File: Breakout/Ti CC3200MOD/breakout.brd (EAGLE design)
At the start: 52.5 x 42.5 mm, 68 parts, among them Q1 16Mhz, U1 TPS63001DRCT, U11 XL, U12 TMP006, U2 MCP73871-2CCI/ML, U5 93LC46BT-I/OT

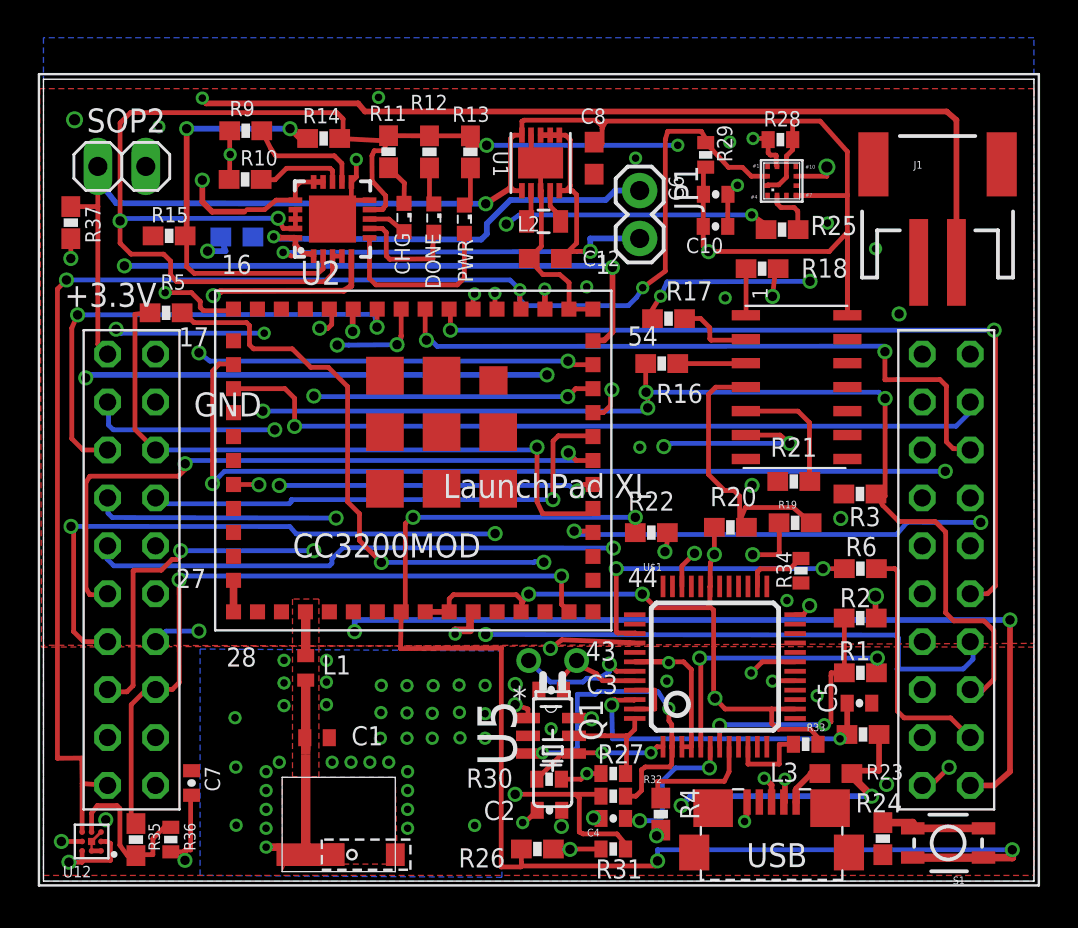
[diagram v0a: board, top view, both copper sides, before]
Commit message: Revert "Add Power Jumper"
This reverts commit 700f51e2ac70f058cb62d27b6654cd07e4fedc2f.
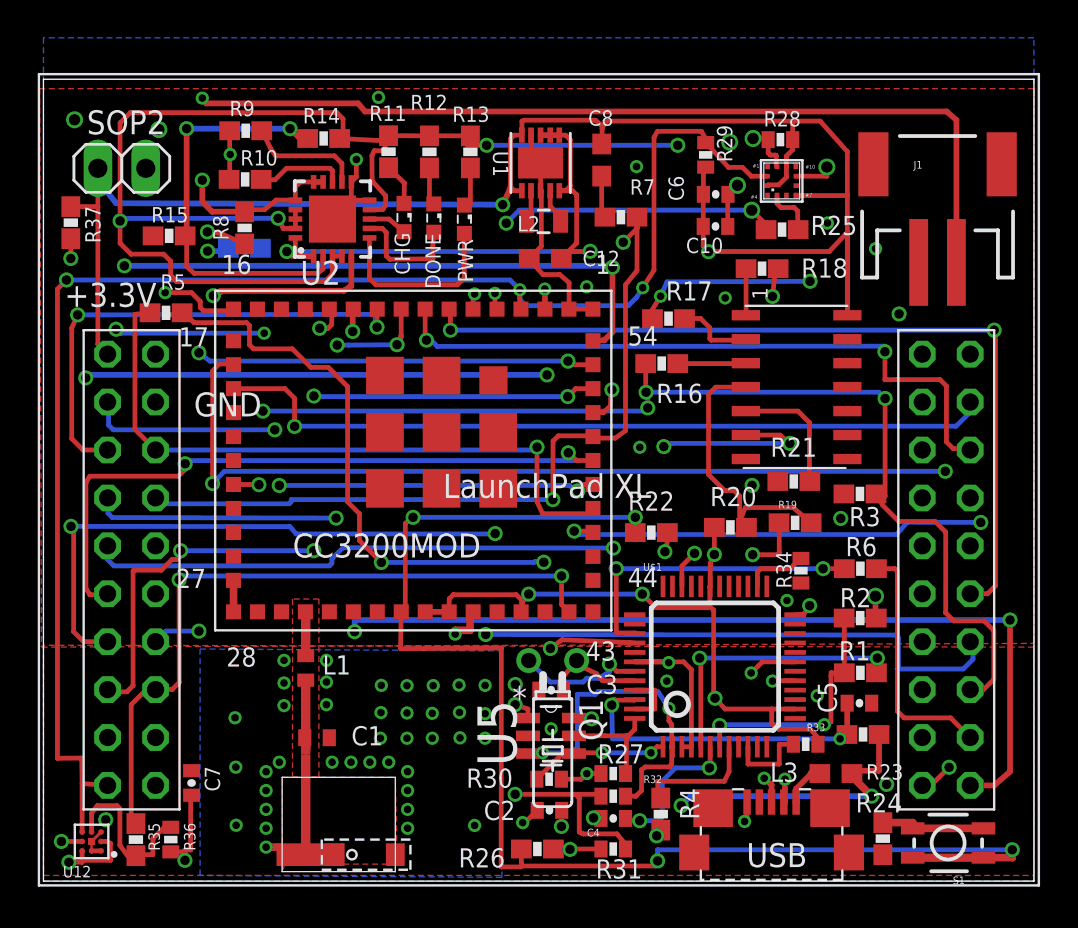
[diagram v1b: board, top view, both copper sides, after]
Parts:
- removed JP1: (no value), DECADE-libraries:1X02
- added R7: 100K, SparkFun-Resistors:0603-RES
- added R8: 470K, SparkFun-Resistors:0603-RES
- moved THERMAL 0.72 mm to (22.6, 33.5)
- moved C8 0.41 mm to (41.6, 38.2)
- moved SOP2 0.10 mm to (16.2, 37.8)
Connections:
- removed net OUT_SWCH: JP1.1, U2.1, U2.20
- net +BATT: now also R8.2
- net GND: now also R7.1
- net GPIO_05: now also R7.2, R8.1
- net OUT: now also U2.1, U2.20; no longer JP1.2
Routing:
- net GPIO_05: track 26.8 -> 66.1 mm, vias 1 -> 3
- net OUT_SWCH: track 23.6 -> 0.00 mm, vias 1 -> 0
- net GND: track 43.0 -> 45.2 mm
- net OUT: track 31.3 -> 30.6 mm
- net N$28: track 13.8 -> 13.2 mm

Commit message: Add Power Jumper
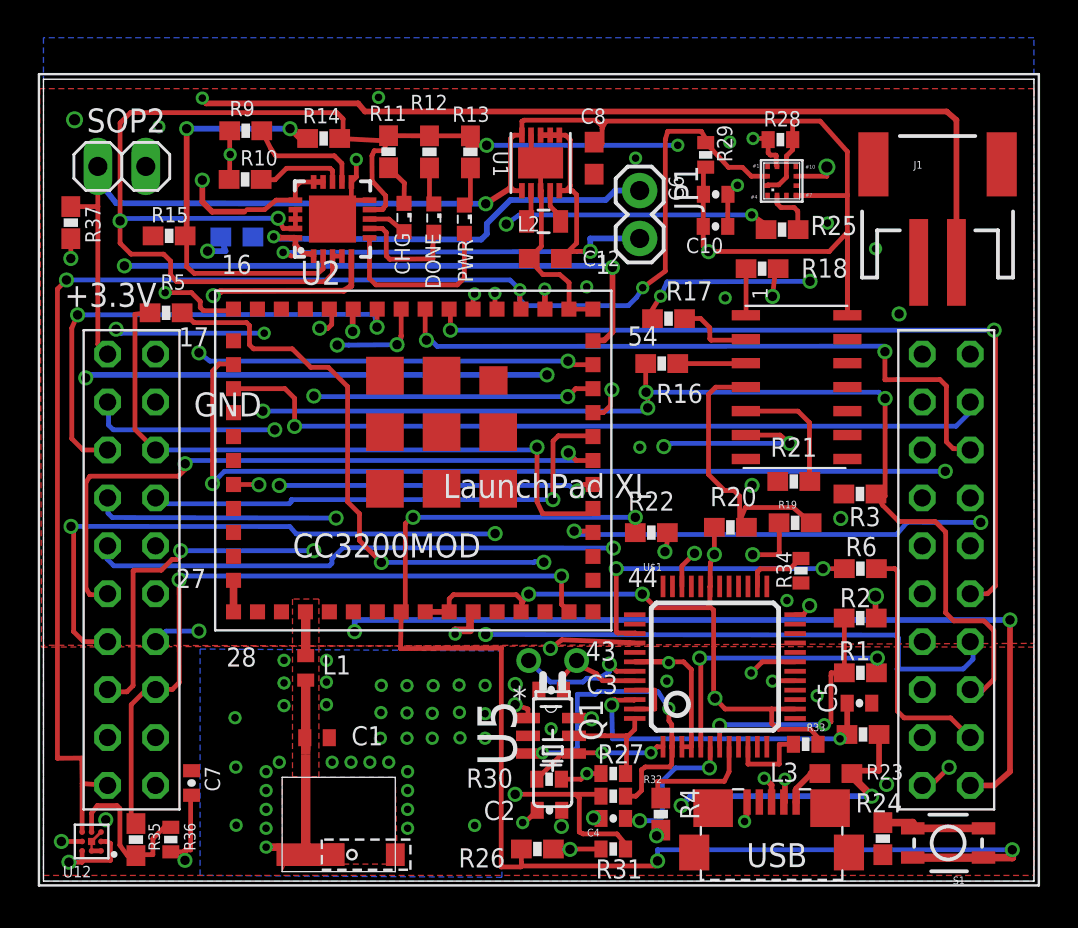
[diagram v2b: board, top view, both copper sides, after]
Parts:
- removed R7: 100K, SparkFun-Resistors:0603-RES
- removed R8: 470K, SparkFun-Resistors:0603-RES
- added JP1: (no value), DECADE-libraries:1X02
- moved THERMAL 0.72 mm to (22.2, 34.1)
- moved C8 0.41 mm to (41.2, 38.3)
- moved SOP2 0.10 mm to (16.2, 37.9)
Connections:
- new net OUT_SWCH: JP1.1, U2.1, U2.20
- net +BATT: no longer R8.2
- net GND: no longer R7.1
- net GPIO_05: no longer R7.2, R8.1
- net OUT: now also JP1.2; no longer U2.1, U2.20
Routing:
- net GPIO_05: track 66.1 -> 26.8 mm, vias 3 -> 1
- net OUT_SWCH: track 0.00 -> 23.6 mm, vias 0 -> 1
- net GND: track 45.2 -> 43.0 mm
- net OUT: track 30.6 -> 31.3 mm
- net N$28: track 13.2 -> 13.8 mm
